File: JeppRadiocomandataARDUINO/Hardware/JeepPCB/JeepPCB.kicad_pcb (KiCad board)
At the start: 2 copper layers, 43 x 48.2 mm, 21 parts, among them J1 Radio, U1 ATmega328P-A, Y1 Crystal

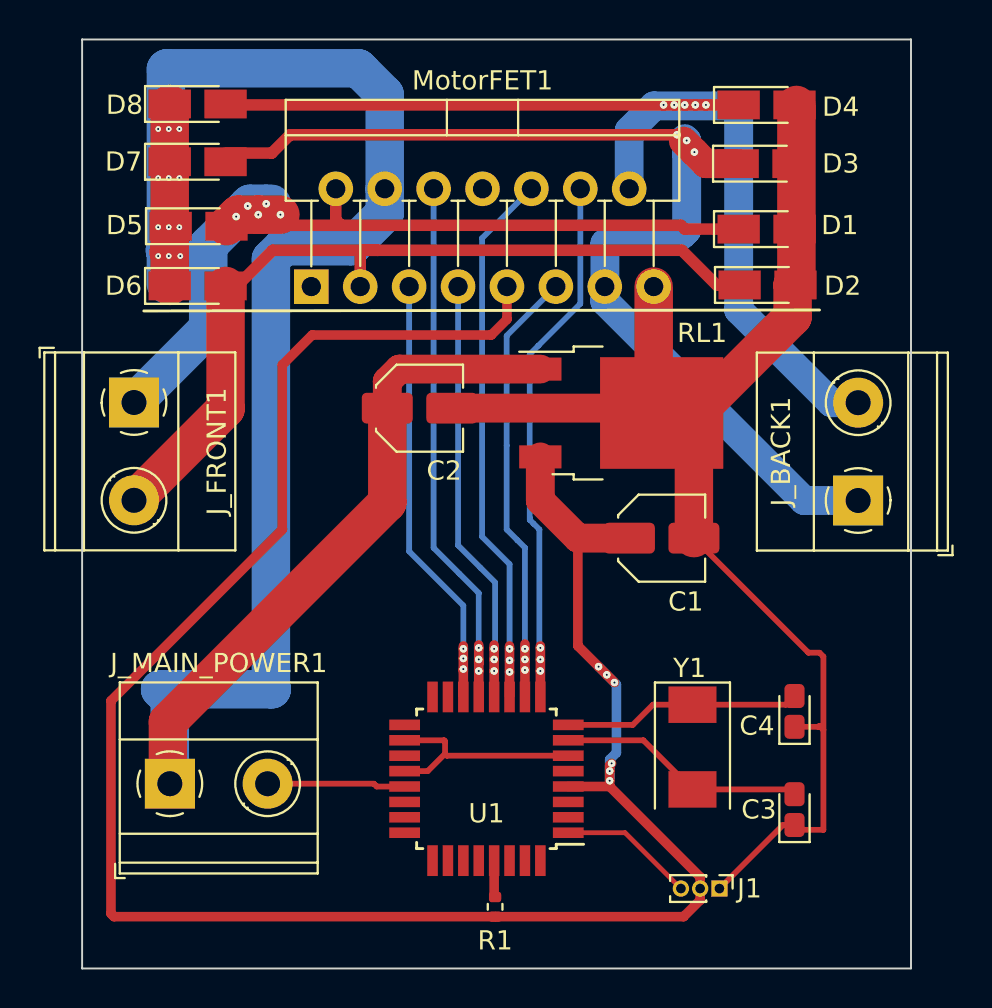
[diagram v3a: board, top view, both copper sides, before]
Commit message: Aggiornamento del PCB aggiunta di VCC e di Vie
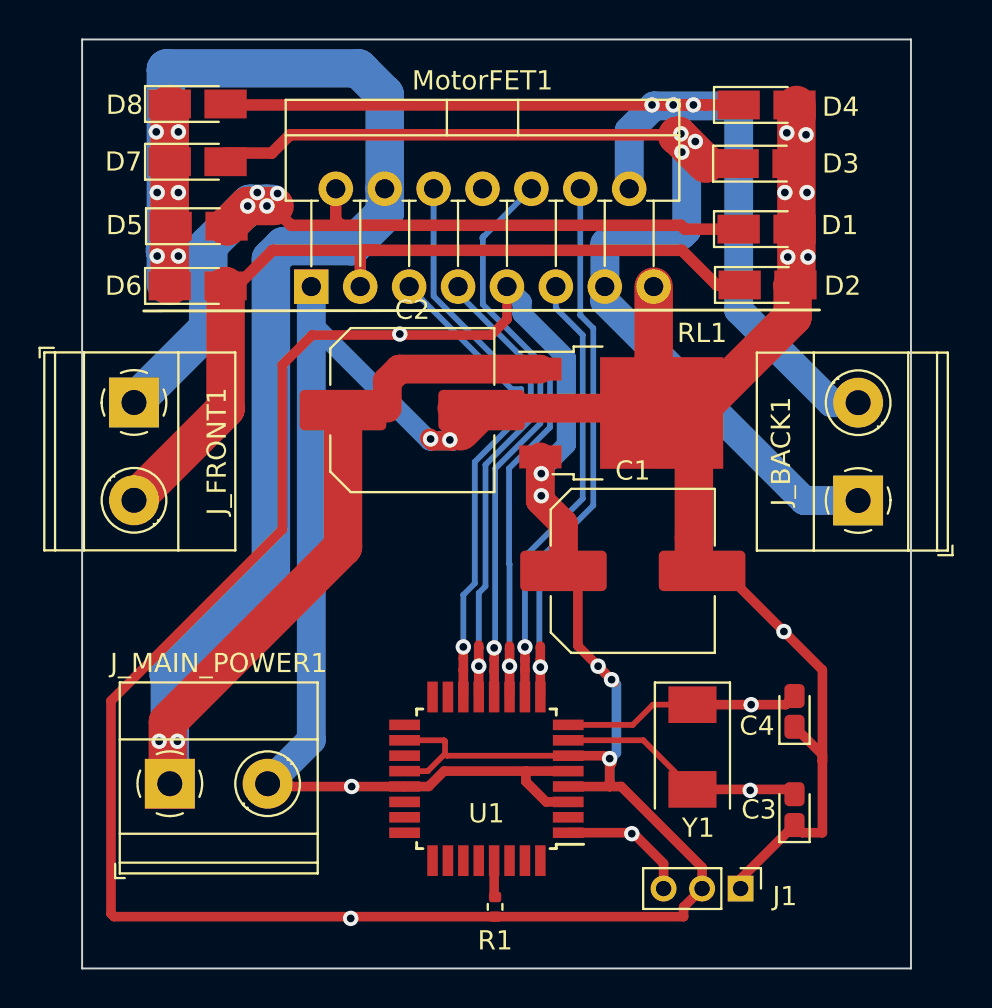
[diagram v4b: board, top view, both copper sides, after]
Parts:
- C1, C2: footprint Capacitor_SMD:C_Elec_4x5.8 -> Capacitor_SMD:C_Elec_8x10.2
- J1: footprint Connector_PinHeader_1.00mm:PinHeader_1x03_P1.00mm_Vertical -> Connector_PinHeader_2.00mm:PinHeader_1x03_P2.00mm_Vertical
- moved C1 2.27 mm to (68.6, 67.2)
- moved J1 1.10 mm to (74.2, 83.7)
- moved C2 0.39 mm to (57.1, 58.9)
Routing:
- net Earth: track 78.8 -> 136.0 mm, vias 0 -> 10
- net VCC: track 122.9 -> 136.7 mm, vias 6 -> 7
- net /5-12V: track 112.8 -> 108.0 mm, vias 12 -> 8
- net INO_D10: track 24.0 -> 26.8 mm, vias 3 -> 1
- net INO_D9: track 29.2 -> 31.8 mm, vias 3 -> 1
- net INO_D8: track 23.7 -> 25.7 mm, vias 3 -> 1
- net INO_D7: track 29.4 -> 31.3 mm, vias 3 -> 1
- net INO_D6: track 24.3 -> 24.7 mm, vias 3 -> 1
- net INO_D5: track 29.2 -> 29.3 mm, vias 3 -> 1
- net Net-(J1-Pad3): track 7.05 -> 6.91 mm, vias 0 -> 1
- net Net-(D1-Pad1): track 43.3 -> 43.1 mm, vias 5 -> 4
- net Net-(D4-Pad1): vias 5 -> 3
- net Net-(C4-Pad2): vias 0 -> 1
- net Net-(C3-Pad2): vias 0 -> 1
